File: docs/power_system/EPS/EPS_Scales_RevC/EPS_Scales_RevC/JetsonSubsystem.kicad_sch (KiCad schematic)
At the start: 25 parts, among them J11 G125-MH11605L3P, U4 INA230

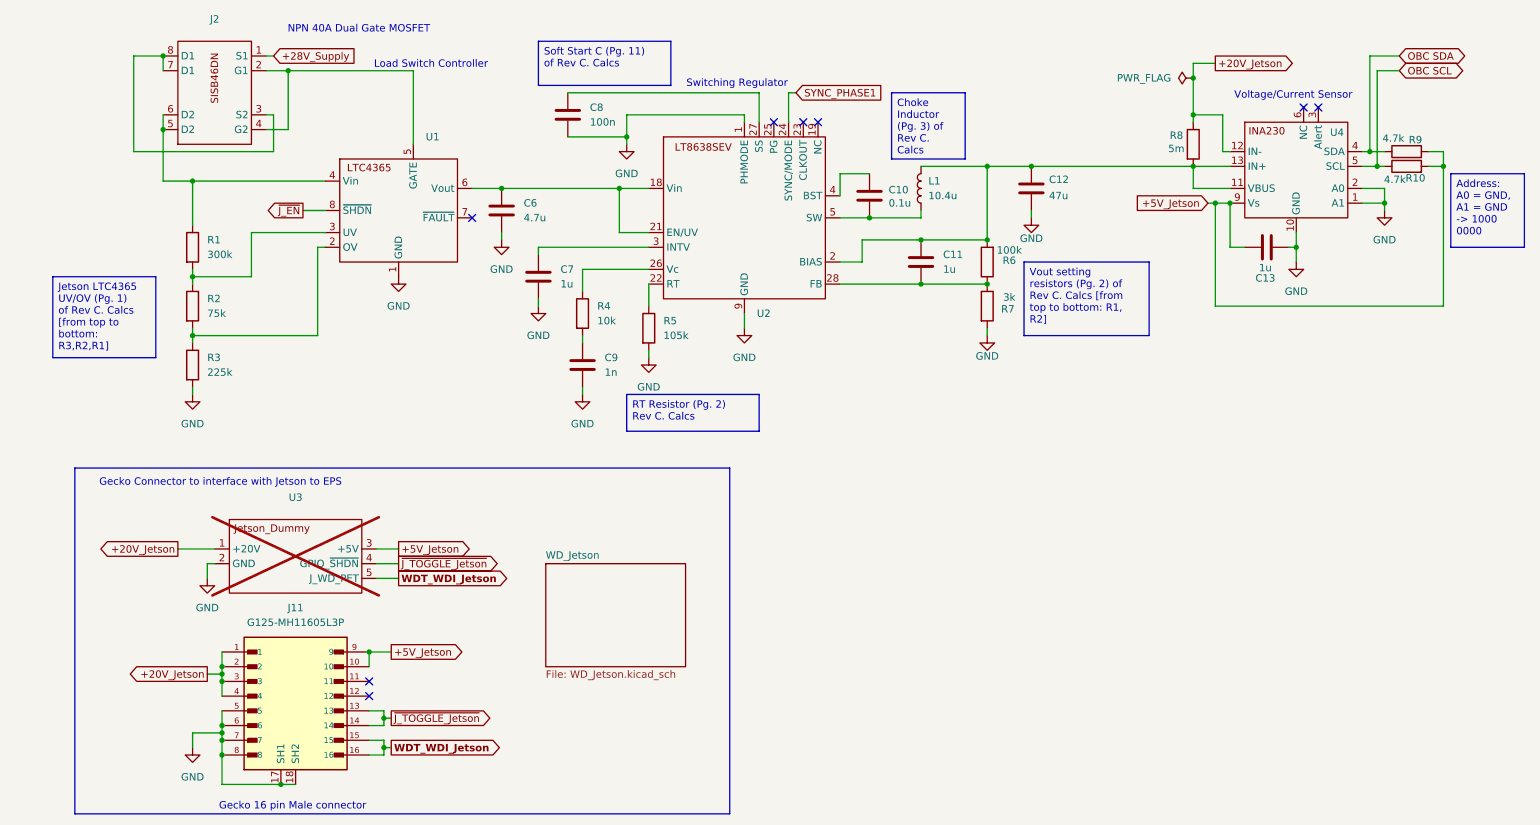
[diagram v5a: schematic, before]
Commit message: WIP REV C. Layout
Completed primary routing configuration.
Current orientation of components is for prototyping and does not reflect final layout.
Need further DRC checkings and track size correction for each sub-system.
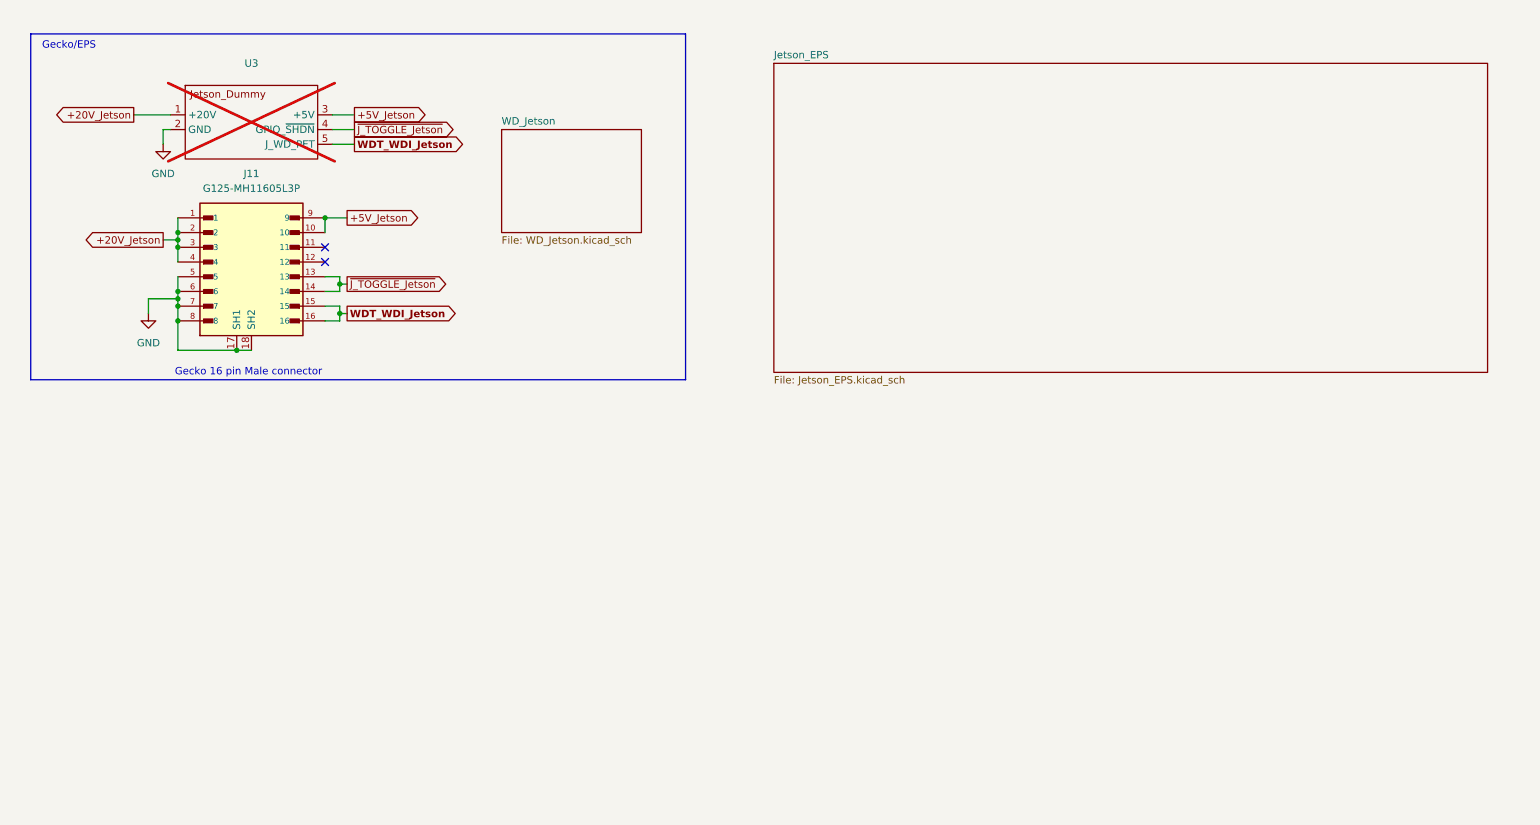
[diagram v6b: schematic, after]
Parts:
- removed C10: 0.1u, Capacitor_SMD:C_0603_1608Metric, symbol Device:C
- removed C11, C13, C7: 1u, Capacitor_SMD:C_0603_1608Metric, symbol Device:C
- removed C12: 47u, Capacitor_SMD:C_0603_1608Metric, symbol Device:C
- removed C6: 4.7u, Capacitor_SMD:C_0603_1608Metric, symbol Device:C
- removed C8: 100n, Capacitor_SMD:C_0603_1608Metric, symbol Device:C
- removed C9: 1n, Capacitor_SMD:C_0603_1608Metric, symbol Device:C
- removed J2: ~, RevC Footprints:SISB46DN-T1-GE3, symbol SISB46DN:SISB46DN
- removed L1: 10.4u, Inductor_SMD:L_0603_1608Metric, symbol Device:L
- removed R1: 300k, Resistor_SMD:R_0603_1608Metric, symbol Device:R
- removed R10, R9: 4.7k, Resistor_SMD:R_0603_1608Metric, symbol Device:R
- removed R2: 75k, Resistor_SMD:R_0603_1608Metric, symbol Device:R
- removed R3: 225k, Resistor_SMD:R_0603_1608Metric, symbol Device:R
- removed R4: 10k, Resistor_SMD:R_0603_1608Metric, symbol Device:R
- removed R5: 105k, Resistor_SMD:R_0603_1608Metric, symbol Device:R
- removed R6: 100k, Resistor_SMD:R_0603_1608Metric, symbol Device:R
- removed R7: 3k, Resistor_SMD:R_0603_1608Metric, symbol Device:R
- removed R8: 5m, Resistor_SMD:R_0603_1608Metric, symbol Device:R
- removed U1: ~, RevC Footprints:LTC4365, symbol LTC4365:LTC4365
- removed U2: ~, RevC Footprints:LT8638SEVPBF, symbol LT8638SEV#PBF:LT863SEV#PBF
- removed U4: INA230, RevC Footprints:INA230AIRGTT, symbol INA230:INA230 [RGT PACKAGE]
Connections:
- no-connect marks 8 -> 2
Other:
- added sheet Jetson_EPS (Jetson_EPS.kicad_sch)
- note added: "Gecko/EPS"
- note removed: "Gecko Connector to interface with Jetson to EPS"
- note removed: "Load Switch Controller"
- note removed: "NPN 40A Dual Gate MOSFET"
- note removed: "Switching Regulator"
- note removed: "Voltage/Current Sensor"
- moved on the sheet: J11, U3

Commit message: WIP EPS REV C.
Removed XNOR implementation, redid layout for compactness, restarting routing for more efficient traces.
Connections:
- net ~{J_TOGGLE_Jetson}: no longer J11.13, J11.14
- no-connect marks 2 -> 4
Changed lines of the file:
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@@
-	)
-	(junction
-		(at 69.85 60.96)
-		(diameter 0)
-		(color 0 0 0 0)
 	)
 	(junction
@@
 	)
 	(no_connect
+		(at 67.31 62.23)
+	)
+	(no_connect
+		(at 67.31 59.69)
+	)
+	(no_connect
 		(at 67.31 54.61)
 	)
@@
 	(wire
 		(pts
-			(xy 67.31 62.23) (xy 69.85 62.23)
-		)
-		(stroke
-			(width 0)
-			(type default)
-		)
-	)
-	(wire
-		(pts
 			(xy 41.91 54.61) (xy 41.91 57.15)
 		)
@@
 	(wire
 		(pts
-			(xy 69.85 60.96) (xy 71.12 60.96)
-		)
-		(stroke
-			(width 0)
-			(type default)
-		)
-	)
-	(wire
-		(pts
 			(xy 67.31 49.53) (xy 71.12 49.53)
 		)
@@
 	(wire
 		(pts
-			(xy 69.85 59.69) (xy 69.85 60.96)
-		)
-		(stroke
-			(width 0)
-			(type default)
-		)
-	)
-	(wire
-		(pts
 			(xy 41.91 64.77) (xy 41.91 67.31)
 		)
@@
 	(wire
 		(pts
-			(xy 69.85 62.23) (xy 69.85 60.96)
-		)
-		(stroke
-			(width 0)
-			(type default)
-		)
-	)
-	(wire
-		(pts
 			(xy 39.37 36.83) (xy 39.37 34.29)
 		)
@@
 		(pts
 			(xy 36.83 63.5) (xy 41.91 63.5)
-		)
-		(stroke
-			(width 0)
-			(type default)
-		)
-	)
-	(wire
-		(pts
-			(xy 67.31 59.69) (xy 69.85 59.69)
 		)
 		(stroke
@@
 			(effects
 				(font
-					(size 1.27 1.27)
-				)
-				(justify left)
-				(hide yes)
-			)
-		)
-	)
-	(global_label "~{J_TOGGLE_Jetson}"
-		(shape output)
-		(at 71.12 60.96 0)
-		(fields_autoplaced yes)
-		(effects
-			(font
-				(size 1.27 1.27)
-			)
-			(justify left)
-		)
-		(property "Intersheetrefs" "${INTERSHEET_REFS}"
-			(at 90.1312 60.96 0)
-			(effects
-				(font

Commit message: Layout and Routing DONE
Layout and Routing is complete, next step is DRC checking and making sure that the tracks and fab settings coincide with the settings we want to manufacture with.  Worth noting that we should probably get a version of this board with just one subsystem to test first before buying the whole thing.
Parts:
- J11: footprint RevC Footprints:HARWIN_G125-MH11605L3P -> RevC Footprints:CON16_2X8_UF_DF11
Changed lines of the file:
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@@
 			)
 		)
-		(property "Footprint" "RevC Footprints:HARWIN_G125-MH11605L3P"
+		(property "Footprint" "RevC Footprints:CON16_2X8_UF_DF11"
 			(at 54.61 59.69 0)
 			(effects
